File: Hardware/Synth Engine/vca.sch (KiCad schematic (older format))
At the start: 73 parts, among them Q1 MMBT3904-TP, Q2 MMBT3904-TP, Q3 MMBT3904-TP, Q4 MMBT3904-TP, Q5 MMBFJ177, Q6 MMBFJ177, Q7 MMBFJ177, Q8 MMBFJ177, U2 TL074

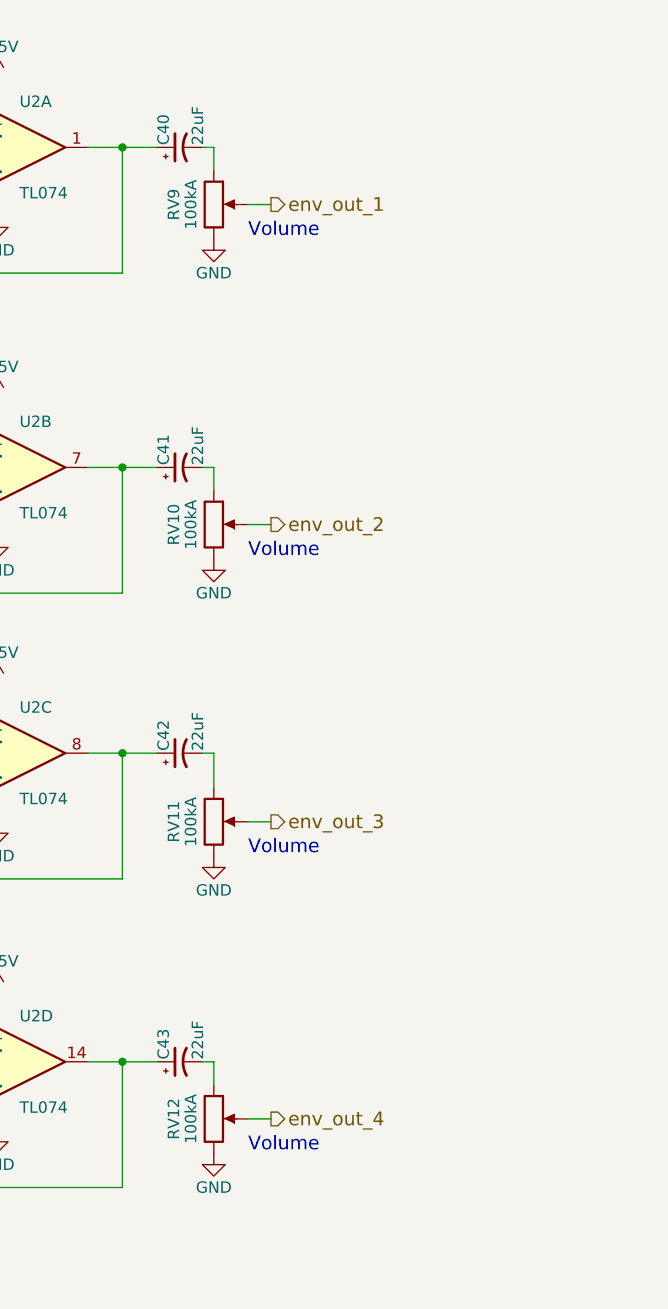
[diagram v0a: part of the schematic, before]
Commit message: add volume pots to control board
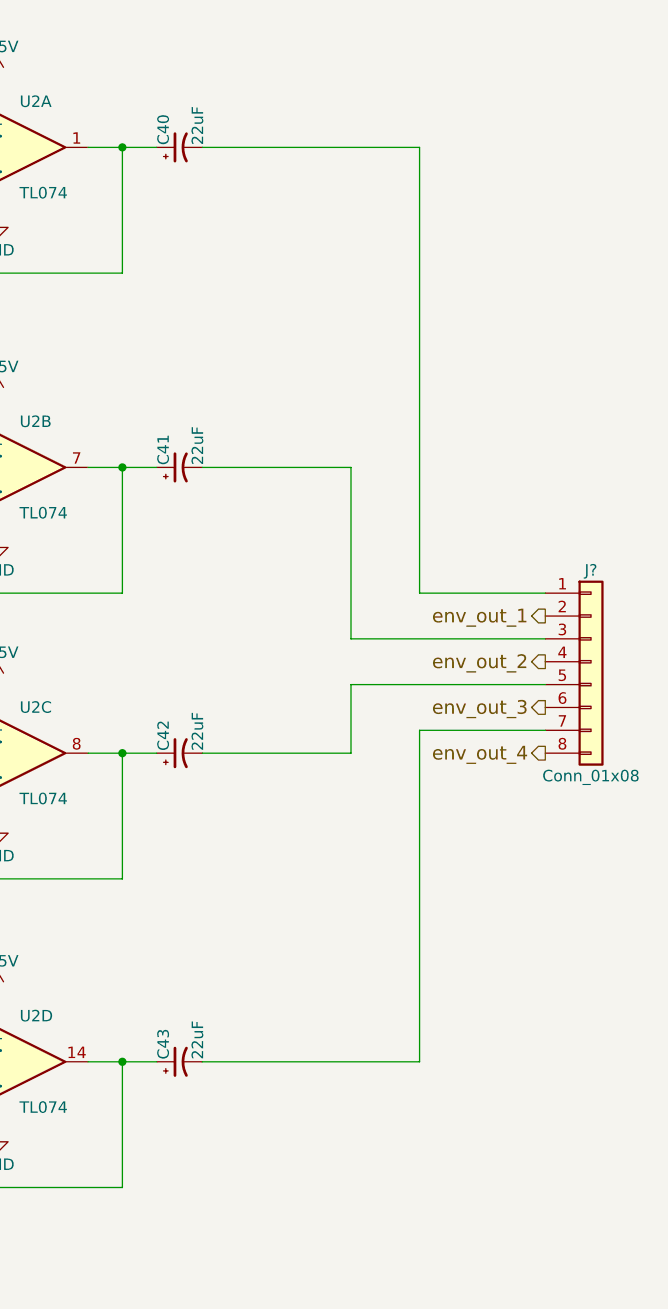
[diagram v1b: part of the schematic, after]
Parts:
- removed RV10, RV11, RV12, RV9: 100kA, Potentiometers:Potentiometer_Bourns_PTV09A-1_Horizontal, symbol POT
- added J?: Conn_01x08, symbol Conn_01x08
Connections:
- net env_out_1: now also J?.2 (Pin_2)
- net env_out_2: now also J?.4 (Pin_4)
- net env_out_3: now also J?.6 (Pin_6)
- net env_out_4: now also J?.8 (Pin_8)
- net at C40.2: now also J?.1 (Pin_1)
- net at C41.2: now also J?.3 (Pin_3)
- net at C42.2: now also J?.5 (Pin_5)
- net at C43.2: now also J?.7 (Pin_7)
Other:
- note removed: "Volume"
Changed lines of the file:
@@
 Text HLabel 5400 1900 0    60   Input ~ 0
 level1
-Text HLabel 9450 1700 2    60   Output ~ 0
+Text HLabel 10650 3500 0    60   Output ~ 0
 env_out_1
 Text HLabel 5750 2750 0    60   Input ~ 0
@@
 Text HLabel 5450 3300 0    60   Input ~ 0
 level2
-Text HLabel 9450 3100 2    60   Output ~ 0
+Text HLabel 10650 3700 0    60   Output ~ 0
 env_out_2
 Text HLabel 5750 4000 0    60   Input ~ 0
@@
 Text HLabel 5350 4550 0    60   Input ~ 0
 level3
-Text HLabel 9450 4400 2    60   Output ~ 0
+Text HLabel 10650 3900 0    60   Output ~ 0
 env_out_3
 Text HLabel 5750 5350 0    60   Input ~ 0
@@
 Text HLabel 5350 5900 0    60   Input ~ 0
 level4
-Text HLabel 9450 5700 2    60   Output ~ 0
+Text HLabel 10650 4100 0    60   Output ~ 0
 env_out_4
 $Comp
@@
 	8650 1450 8950 1450
 Wire Wire Line
-	9200 1550 9200 1450
-Wire Wire Line
 	8650 2850 8950 2850
 Wire Wire Line
-	9200 2950 9200 2850
-Wire Wire Line
 	8650 4100 8950 4100
 Wire Wire Line
-	9200 4250 9200 4100
-Wire Wire Line
 	8650 5450 8950 5450
-Wire Wire Line
-	9200 5550 9200 5450
 $Comp
 L R R25
@@
 $EndComp
 $Comp
-L GND #PWR038
-U 1 1 5C3BC62F
-P 9200 1850
-F 0 "#PWR038" H 9200 1600 50  0001 C CNN
-F 1 "GND" H 9200 1700 50  0000 C CNN
-F 2 "" H 9200 1850 50  0001 C CNN
-F 3 "" H 9200 1850 50  0001 C CNN
-	1    9200 1850
-	1    0    0    -1
-$EndComp
-$Comp
-L GND #PWR039
-U 1 1 5C3BC6C4
-P 9200 3250
-F 0 "#PWR039" H 9200 3000 50  0001 C CNN
-F 1 "GND" H 9200 3100 50  0000 C CNN
-F 2 "" H 9200 3250 50  0001 C CNN
-F 3 "" H 9200 3250 50  0001 C CNN
-	1    9200 3250
-	1    0    0    -1
-$EndComp
-$Comp
 L GND #PWR040
 U 1 1 5C3BC759
@@
 F 3 "" H 7050 4650 50  0001 C CNN
 	1    7050 4650
-	1    0    0    -1
-$EndComp
-$Comp
-L GND #PWR042
-U 1 1 5C3BC883
-P 9200 4550
-F 0 "#PWR042" H 9200 4300 50  0001 C CNN
-F 1 "GND" H 9200 4400 50  0000 C CNN
-F 2 "" H 9200 4550 50  0001 C CNN
-F 3 "" H 9200 4550 50  0001 C CNN
-	1    9200 4550
-	1    0    0    -1
-$EndComp
-$Comp
-L GND #PWR043
-U 1 1 5C3BC918
-P 9200 5850
-F 0 "#PWR043" H 9200 5600 50  0001 C CNN
-F 1 "GND" H 9200 5700 50  0000 C CNN
-F 2 "" H 9200 5850 50  0001 C CNN
-F 3 "" H 9200 5850 50  0001 C CNN
-	1    9200 5850
 	1    0    0    -1
 $EndComp
@@
 	0    1    1    0
 $EndComp
-$Comp
-L POT RV9
-U 1 1 5C3D05BD
-P 9200 1700
-F 0 "RV9" V 9025 1700 50  0000 C CNN
-F 1 "100kA" V 9100 1700 50  0000 C CNN
-F 2 "Potentiometers:Potentiometer_Bourns_PTV09A-1_Horizontal" H 9200 1700 50  0001 C CNN
-F 3 "" H 9200 1700 50  0001 C CNN
-	1    9200 1700
-	1    0    0    -1
-$EndComp
-Wire Wire Line
-	9450 1700 9350 1700
-Wire Wire Line
-	9200 1450 9150 1450
-$Comp
-L POT RV10
-U 1 1 5C3D0AB4
-P 9200 3100
-F 0 "RV10" V 9025 3100 50  0000 C CNN
-F 1 "100kA" V 9100 3100 50  0000 C CNN
-F 2 "Potentiometers:Potentiometer_Bourns_PTV09A-1_Horizontal" H 9200 3100 50  0001 C CNN
-F 3 "" H 9200 3100 50  0001 C CNN
-	1    9200 3100
-	1    0    0    -1
-$EndComp
-$Comp
-L POT RV11
-U 1 1 5C3D0C1E
-P 9200 4400
-F 0 "RV11" V 9025 4400 50  0000 C CNN
-F 1 "100kA" V 9100 4400 50  0000 C CNN
-F 2 "Potentiometers:Potentiometer_Bourns_PTV09A-1_Horizontal" H 9200 4400 50  0001 C CNN
-F 3 "" H 9200 4400 50  0001 C CNN
-	1    9200 4400
-	1    0    0    -1
-$EndComp
-$Comp
-L POT RV12
-U 1 1 5C3D0DC0
-P 9200 5700
-F 0 "RV12" V 9025 5700 50  0000 C CNN
-F 1 "100kA" V 9100 5700 50  0000 C CNN
-F 2 "Potentiometers:Potentiometer_Bourns_PTV09A-1_Horizontal" H 9200 5700 50  0001 C CNN
-F 3 "" H 9200 5700 50  0001 C CNN
-	1    9200 5700
-	1    0    0    -1
-$EndComp
-Wire Wire Line
-	9450 3100 9350 3100
-Wire Wire Line
-	9200 2850 9150 2850
-Wire Wire Line
-	9450 4400 9350 4400
-Wire Wire Line
-	9200 4100 9150 4100
-Wire Wire Line
-	9450 5700 9350 5700
-Wire Wire Line
-	9200 5450 9150 5450
-Text Notes 9350 1850 0    60   ~ 0
-Volume
-Text Notes 9350 3250 0    60   ~ 0
-Volume
-Text Notes 9350 4550 0    60   ~ 0
-Volume
-Text Notes 9350 5850 0    60   ~ 0
-Volume
+Wire Wire Line
+	9150 1450 10100 1450
+Wire Wire Line
+	9150 2850 9800 2850
+Wire Wire Line
+	9150 4100 9800 4100
+Wire Wire Line
+	9150 5450 10100 5450
 $Comp
 L CP1_Small C25
@@
 Wire Wire Line
 	1650 4250 1550 4250
+$Comp
+L Conn_01x08 J?
+U 1 1 5C61FEFD
+P 10850 3700
+F 0 "J?" H 10850 4100 50  0000 C CNN
+F 1 "Conn_01x08" H 10850 3200 50  0000 C CNN
+F 2 "" H 10850 3700 50  0001 C CNN
+F 3 "" H 10850 3700 50  0001 C CNN
+	1    10850 3700
+	1    0    0    -1
+$EndComp
+Wire Wire Line
+	10100 1450 10100 3400
+Wire Wire Line
+	10100 3400 10650 3400
+Wire Wire Line
+	10650 3600 9800 3600
+Wire Wire Line
+	9800 3600 9800 2850
+Wire Wire Line
+	9800 3800 10650 3800
+Wire Wire Line
+	9800 3800 9800 4100
+Wire Wire Line
+	10650 4000 10100 4000
+Wire Wire Line
+	10100 4000 10100 5450
 $EndSCHEMATC

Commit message: remove external pull-up resistors on digital input pins. These are unecessary due to internal pull-up resistors.
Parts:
- J4: renamed from J?; footprint (none) -> Pin_Headers:Pin_Header_Straight_1x08_Pitch2.54mm
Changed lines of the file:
@@
 $EndComp
 $Comp
-L GND #PWR040
+L GND #PWR038
 U 1 1 5C3BC759
 P 7050 3400
-F 0 "#PWR040" H 7050 3150 50  0001 C CNN
+F 0 "#PWR038" H 7050 3150 50  0001 C CNN
 F 1 "GND" H 7050 3250 50  0000 C CNN
 F 2 "" H 7050 3400 50  0001 C CNN
@@
 $EndComp
 $Comp
-L GND #PWR041
+L GND #PWR039
 U 1 1 5C3BC7EE
 P 7050 4650
-F 0 "#PWR041" H 7050 4400 50  0001 C CNN
+F 0 "#PWR039" H 7050 4400 50  0001 C CNN
 F 1 "GND" H 7050 4500 50  0000 C CNN
 F 2 "" H 7050 4650 50  0001 C CNN
@@
 $EndComp
 $Comp
-L GND #PWR044
+L GND #PWR040
 U 1 1 5C3BC9AD
 P 7050 6000
-F 0 "#PWR044" H 7050 5750 50  0001 C CNN
+F 0 "#PWR040" H 7050 5750 50  0001 C CNN
 F 1 "GND" H 7050 5850 50  0000 C CNN
 F 2 "" H 7050 6000 50  0001 C CNN
@@
 $EndComp
 $Comp
-L GND #PWR045
+L GND #PWR041
 U 1 1 5C540E8F
 P 1150 2000
-F 0 "#PWR045" H 1150 1750 50  0001 C CNN
+F 0 "#PWR041" H 1150 1750 50  0001 C CNN
 F 1 "GND" H 1150 1850 50  0000 C CNN
 F 2 "" H 1150 2000 50  0001 C CNN
@@
 $EndComp
 $Comp
-L GND #PWR046
+L GND #PWR042
 U 1 1 5C540E95
 P 1500 2000
-F 0 "#PWR046" H 1500 1750 50  0001 C CNN
+F 0 "#PWR042" H 1500 1750 50  0001 C CNN
 F 1 "GND" H 1500 1850 50  0000 C CNN
 F 2 "" H 1500 2000 50  0001 C CNN
@@
 $EndComp
 $Comp
-L +15V #PWR047
+L +15V #PWR043
 U 1 1 5C540E9B
 P 1150 1300
-F 0 "#PWR047" H 1150 1150 50  0001 C CNN
+F 0 "#PWR043" H 1150 1150 50  0001 C CNN
 F 1 "+15V" H 1150 1440 50  0000 C CNN
 F 2 "" H 1150 1300 50  0001 C CNN
@@
 Connection ~ 1500 1650
 $Comp
-L +15V #PWR048
+L +15V #PWR044
 U 1 1 5C540EAE
 P 1900 1150
-F 0 "#PWR048" H 1900 1000 50  0001 C CNN
+F 0 "#PWR044" H 1900 1000 50  0001 C CNN
 F 1 "+15V" H 1900 1290 50  0000 C CNN
 F 2 "" H 1900 1150 50  0001 C CNN
@@
 $EndComp
 $Comp
-L GND #PWR049
+L GND #PWR045
 U 1 1 5C543B7C
 P 1150 3400
-F 0 "#PWR049" H 1150 3150 50  0001 C CNN
+F 0 "#PWR045" H 1150 3150 50  0001 C CNN
 F 1 "GND" H 1150 3250 50  0000 C CNN
 F 2 "" H 1150 3400 50  0001 C CNN
@@
 $EndComp
 $Comp
-L GND #PWR050
+L GND #PWR046
 U 1 1 5C543B82
 P 1500 3400
-F 0 "#PWR050" H 1500 3150 50  0001 C CNN
+F 0 "#PWR046" H 1500 3150 50  0001 C CNN
 F 1 "GND" H 1500 3250 50  0000 C CNN
 F 2 "" H 1500 3400 50  0001 C CNN
@@
 $EndComp
 $Comp
-L +15V #PWR051
+L +15V #PWR047
 U 1 1 5C543B88
 P 1150 2700
-F 0 "#PWR051" H 1150 2550 50  0001 C CNN
+F 0 "#PWR047" H 1150 2550 50  0001 C CNN
 F 1 "+15V" H 1150 2840 50  0000 C CNN
 F 2 "" H 1150 2700 50  0001 C CNN
@@
 $EndComp
 $Comp
-L GND #PWR052
+L GND #PWR048
 U 1 1 5C543E17
 P 1200 4800
-F 0 "#PWR052" H 1200 4550 50  0001 C CNN
+F 0 "#PWR048" H 1200 4550 50  0001 C CNN
 F 1 "GND" H 1200 4650 50  0000 C CNN
 F 2 "" H 1200 4800 50  0001 C CNN
@@
 $EndComp
 $Comp
-L GND #PWR053
+L GND #PWR049
 U 1 1 5C543E1D
 P 1550 4800
-F 0 "#PWR053" H 1550 4550 50  0001 C CNN
+F 0 "#PWR049" H 1550 4550 50  0001 C CNN
 F 1 "GND" H 1550 4650 50  0000 C CNN
 F 2 "" H 1550 4800 50  0001 C CNN
@@
 $EndComp
 $Comp
-L +15V #PWR054
+L +15V #PWR050
 U 1 1 5C543E23
 P 1200 4100
-F 0 "#PWR054" H 1200 3950 50  0001 C CNN
+F 0 "#PWR050" H 1200 3950 50  0001 C CNN
 F 1 "+15V" H 1200 4240 50  0000 C CNN
 F 2 "" H 1200 4100 50  0001 C CNN
@@
 $EndComp
 $Comp
-L GND #PWR055
+L GND #PWR051
 U 1 1 5C543E54
 P 1200 6200
-F 0 "#PWR055" H 1200 5950 50  0001 C CNN
+F 0 "#PWR051" H 1200 5950 50  0001 C CNN
 F 1 "GND" H 1200 6050 50  0000 C CNN
 F 2 "" H 1200 6200 50  0001 C CNN
@@
 $EndComp
 $Comp
-L GND #PWR056
+L GND #PWR052
 U 1 1 5C543E5A
 P 1550 6200
-F 0 "#PWR056" H 1550 5950 50  0001 C CNN
+F 0 "#PWR052" H 1550 5950 50  0001 C CNN
 F 1 "GND" H 1550 6050 50  0000 C CNN
 F 2 "" H 1550 6200 50  0001 C CNN
@@
 $EndComp
 $Comp
-L +15V #PWR057
+L +15V #PWR053
 U 1 1 5C543E60
 P 1200 5500
-F 0 "#PWR057" H 1200 5350 50  0001 C CNN
+F 0 "#PWR053" H 1200 5350 50  0001 C CNN
 F 1 "+15V" H 1200 5640 50  0000 C CNN
 F 2 "" H 1200 5500 50  0001 C CNN
@@
 $EndComp
 $Comp
-L GND #PWR058
+L GND #PWR054
 U 1 1 5C5499D3
 P 1900 2050
-F 0 "#PWR058" H 1900 1800 50  0001 C CNN
+F 0 "#PWR054" H 1900 1800 50  0001 C CNN
 F 1 "GND" H 1900 1900 50  0000 C CNN
 F 2 "" H 1900 2050 50  0001 C CNN
@@
 Connection ~ 1900 1700
 $Comp
-L +15V #PWR059
+L +15V #PWR055
 U 1 1 5C54A056
 P 1900 2550
-F 0 "#PWR059" H 1900 2400 50  0001 C CNN
+F 0 "#PWR055" H 1900 2400 50  0001 C CNN
 F 1 "+15V" H 1900 2690 50  0000 C CNN
 F 2 "" H 1900 2550 50  0001 C CNN
@@
 $EndComp
 $Comp
-L GND #PWR060
+L GND #PWR056
 U 1 1 5C54A072
 P 1900 3450
-F 0 "#PWR060" H 1900 3200 50  0001 C CNN
+F 0 "#PWR056" H 1900 3200 50  0001 C CNN
 F 1 "GND" H 1900 3300 50  0000 C CNN
 F 2 "" H 1900 3450 50  0001 C CNN
@@
 Connection ~ 1900 3100
 $Comp
-L +15V #PWR061
+L +15V #PWR057
 U 1 1 5C54A855
 P 1950 3950
-F 0 "#PWR061" H 1950 3800 50  0001 C CNN
+F 0 "#PWR057" H 1950 3800 50  0001 C CNN
 F 1 "+15V" H 1950 4090 50  0000 C CNN
 F 2 "" H 1950 3950 50  0001 C CNN
@@
 $EndComp
 $Comp
-L GND #PWR062
+L GND #PWR058
 U 1 1 5C54A871
 P 1950 4850
-F 0 "#PWR062" H 1950 4600 50  0001 C CNN
+F 0 "#PWR058" H 1950 4600 50  0001 C CNN
 F 1 "GND" H 1950 4700 50  0000 C CNN
 F 2 "" H 1950 4850 50  0001 C CNN
@@
 Connection ~ 1950 4500
 $Comp
-L +15V #PWR063
+L +15V #PWR059
 U 1 1 5C54A9CF
 P 1950 5350
-F 0 "#PWR063" H 1950 5200 50  0001 C CNN
+F 0 "#PWR059" H 1950 5200 50  0001 C CNN
 F 1 "+15V" H 1950 5490 50  0000 C CNN
 F 2 "" H 1950 5350 50  0001 C CNN
@@
 $EndComp
 $Comp
-L GND #PWR064
+L GND #PWR060
 U 1 1 5C54A9EB
 P 1950 6250
-F 0 "#PWR064" H 1950 6000 50  0001 C CNN
+F 0 "#PWR060" H 1950 6000 50  0001 C CNN
 F 1 "GND" H 1950 6100 50  0000 C CNN
 F 2 "" H 1950 6250 50  0001 C CNN
@@
 	1650 4250 1550 4250
 $Comp
-L Conn_01x08 J?
+L Conn_01x08 J4
 U 1 1 5C61FEFD
 P 10850 3700
-F 0 "J?" H 10850 4100 50  0000 C CNN
+F 0 "J4" H 10850 4100 50  0000 C CNN
 F 1 "Conn_01x08" H 10850 3200 50  0000 C CNN
-F 2 "" H 10850 3700 50  0001 C CNN
+F 2 "Pin_Headers:Pin_Header_Straight_1x08_Pitch2.54mm" H 10850 3700 50  0001 C CNN
 F 3 "" H 10850 3700 50  0001 C CNN
 	1    10850 3700
@@
 	9800 3800 10650 3800
 Wire Wire Line
-	9800 3800 9800 4100
+	9800 4100 9800 3800
 Wire Wire Line
 	10650 4000 10100 4000

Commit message: route connectors on control board. Will add additional set of connectors for filter knobs to simplify routing.
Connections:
- net at C36.1, R50.1: now also U2.5 (+); no longer U2.3 (+)
- net at C37.1, R47.1: now also U2.3 (+); no longer U2.5 (+)
- new net: C40.1, U2.6 (-), U2.7
- new net: C41.1, U2.1, U2.2 (-)
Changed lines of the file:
@@
 $Comp
 L TL074 U2
-U 1 1 5C359D57
+U 2 1 5C359D57
 P 8350 1450
 F 0 "U2" H 8350 1650 50  0000 L CNN
@@
 F 2 "digikey-footprints:SOIC-14_W3.9mm" H 8300 1550 50  0001 C CNN
 F 3 "" H 8400 1650 50  0001 C CNN
-	1    8350 1450
+	2    8350 1450
 	1    0    0    -1
 $EndComp
@@
 $Comp
 L TL074 U2
-U 2 1 5C36E8E5
+U 1 1 5C36E8E5
 P 8350 2850
 F 0 "U2" H 8350 3050 50  0000 L CNN
@@
 F 2 "digikey-footprints:SOIC-14_W3.9mm" H 8300 2950 50  0001 C CNN
 F 3 "" H 8400 3050 50  0001 C CNN
-	2    8350 2850
+	1    8350 2850
 	1    0    0    -1
 $EndComp

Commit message: fix LFO connector schem
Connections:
- net at C38.1, R48.1: now also U2.12 (+); no longer U2.10 (+)
- net at C39.1, R49.1: now also U2.10 (+); no longer U2.12 (+)
- new net: C42.1, U2.13 (-), U2.14
- new net: C43.1, U2.8, U2.9 (-)
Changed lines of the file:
@@
 $Comp
 L TL074 U2
-U 3 1 5C36E9DD
+U 4 1 5C36E9DD
 P 8350 4100
 F 0 "U2" H 8350 4300 50  0000 L CNN
@@
 F 2 "digikey-footprints:SOIC-14_W3.9mm" H 8300 4200 50  0001 C CNN
 F 3 "" H 8400 4300 50  0001 C CNN
-	3    8350 4100
+	4    8350 4100
 	1    0    0    -1
 $EndComp
@@
 $Comp
 L TL074 U2
-U 4 1 5C36EAD5
+U 3 1 5C36EAD5
 P 8350 5450
 F 0 "U2" H 8350 5650 50  0000 L CNN
@@
 F 2 "digikey-footprints:SOIC-14_W3.9mm" H 8300 5550 50  0001 C CNN
 F 3 "" H 8400 5650 50  0001 C CNN
-	4    8350 5450
+	3    8350 5450
 	1    0    0    -1
 $EndComp
